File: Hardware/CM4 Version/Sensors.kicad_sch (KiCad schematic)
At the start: 35 parts, among them J10 Conn_01x04, J11 Conn_01x06, J12 TSW-101-08-G-T-RA, J16 Conn_01x03_Female, J4 32K101-400L5, J5 TSW-101-08-G-T-RA, J6 TSW-101-08-G-T-RA, J7 TSW-101-08-G-T-RA, J8 TSW-101-08-G-T-RA, J9 Conn_01x02, Q2 BC817W, U1 BMP280, U2 MAX-M8Q, U3 LSM9DS1

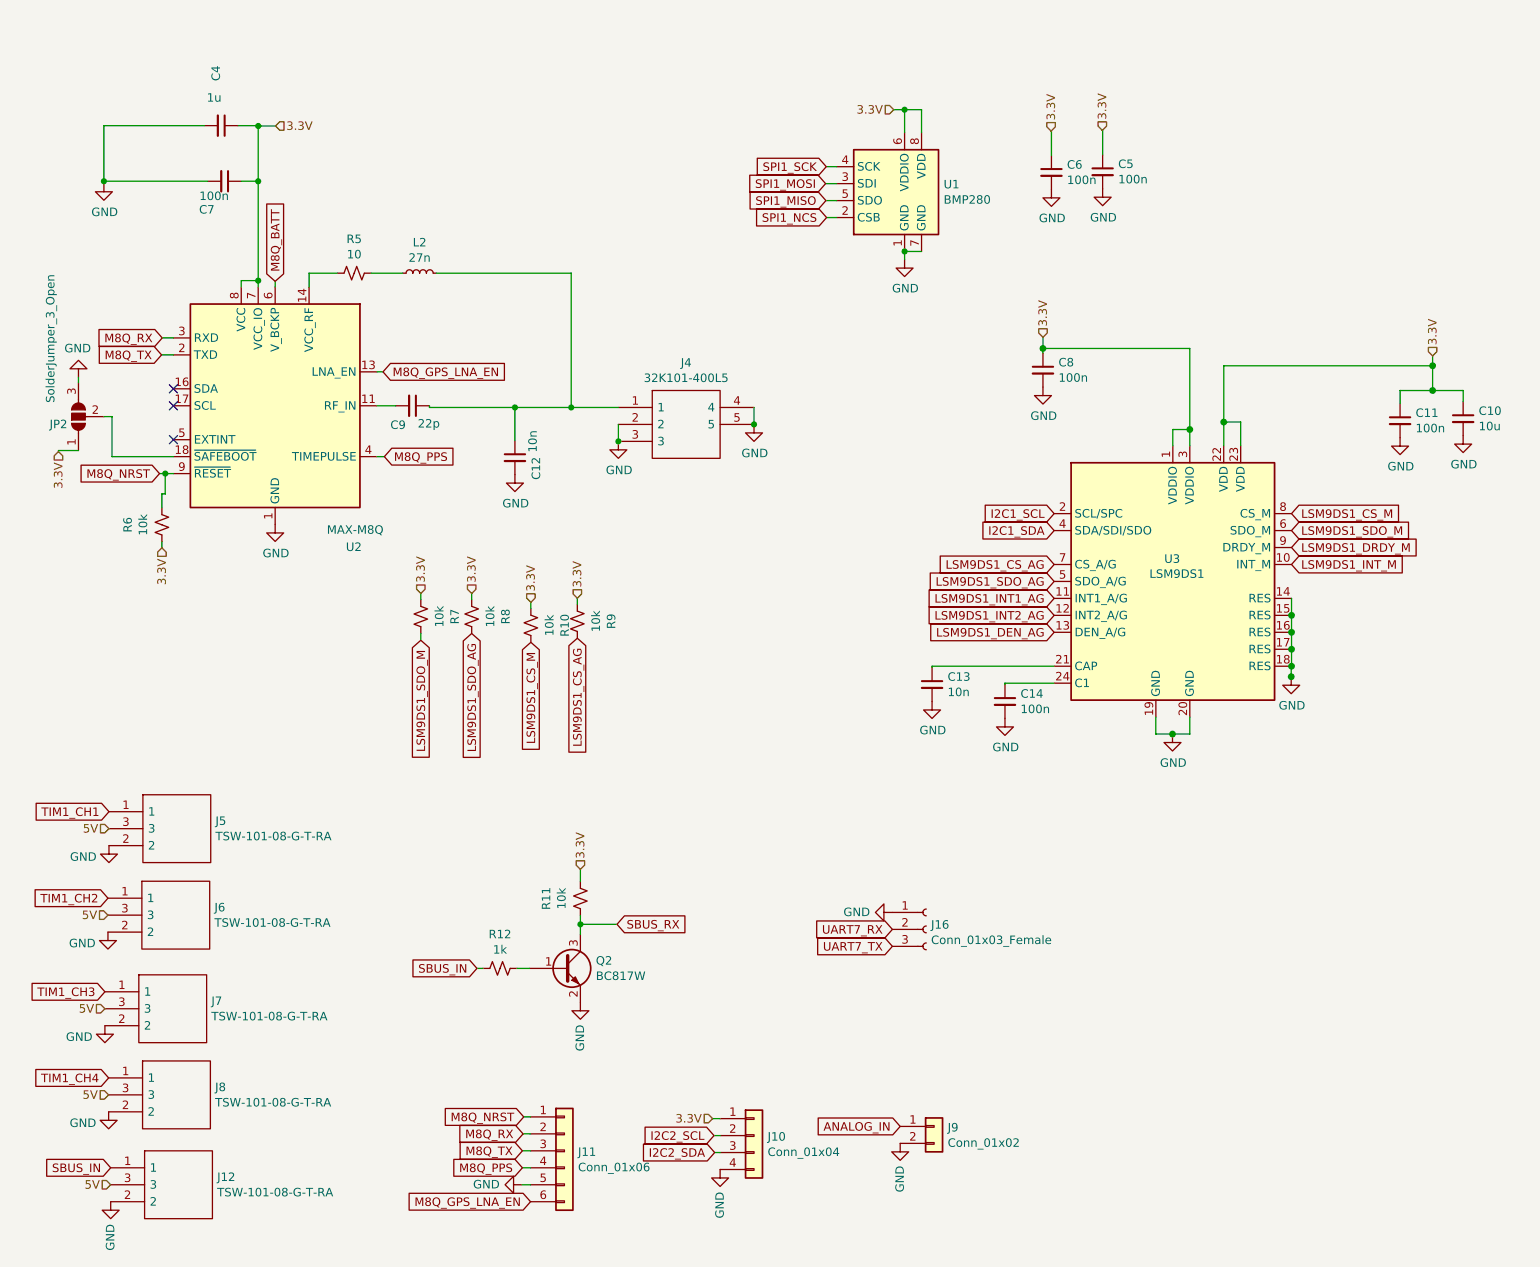
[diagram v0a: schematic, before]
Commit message: Remove CM4-Backups
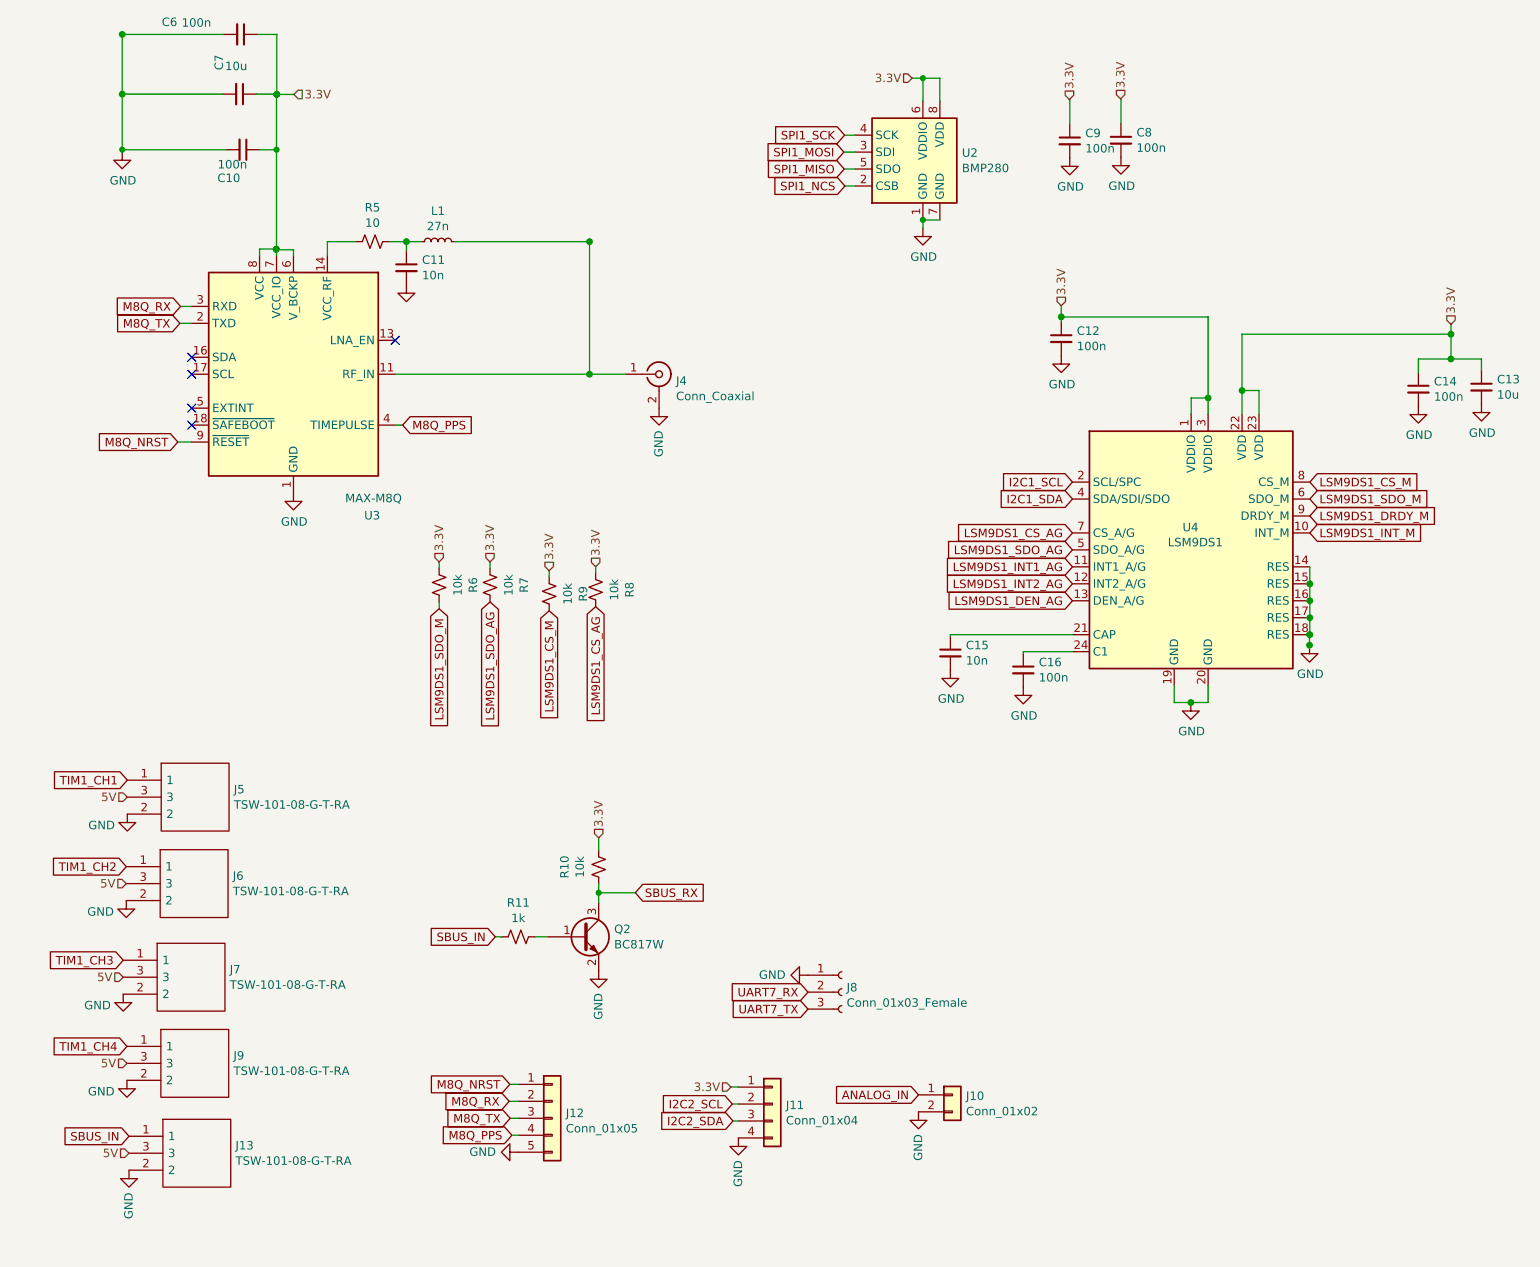
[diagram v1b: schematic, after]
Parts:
- removed C4: 1u, Capacitor_SMD:C_0603_1608Metric, symbol Device:C_Small
- removed C5: 100n, Capacitor_SMD:C_0402_1005Metric, symbol Device:C_Small
- removed J10: Conn_01x04, Connector_Molex:Molex_PicoBlade_53261-0471_1x04-1MP_P1.25mm_Horizontal, symbol Connector_Generic:Conn_01x04
- removed J11: Conn_01x06, Connector_Molex:Molex_PicoBlade_53261-0671_1x06-1MP_P1.25mm_Horizontal, symbol Connector_Generic:Conn_01x06
- removed J12, J8: TSW-101-08-G-T-RA, SamacSys_Parts:HDRRA3W64P254_3X1_254X254X810P, symbol SamacSys_Parts:HTSW-101-08-G-T-RA
- removed J16: Conn_01x03_Female, Connector_PinHeader_2.54mm:PinHeader_1x03_P2.54mm_Vertical, symbol Connector:Conn_01x03_Female
- removed J4: 32K101-400L5, SamacSys_Parts:32K101-400L5, symbol SamacSys_Parts:32K101-400L5
- removed J9: Conn_01x02, Connector_Molex:Molex_PicoBlade_53048-0210_1x02_P1.25mm_Horizontal, symbol Connector_Generic:Conn_01x02
- removed JP2: SolderJumper_3_Open, Jumper:SolderJumper-3_P1.3mm_Open_RoundedPad1.0x1.5mm, symbol Jumper:SolderJumper_3_Open
- removed L2: 27n, Inductor_SMD:L_0402_1005Metric_Pad0.77x0.64mm_HandSolder, symbol Device:L_Small
- removed R12: 1k, Resistor_SMD:R_0402_1005Metric, symbol Device:R_Small_US
- removed U1: BMP280, Package_LGA:Bosch_LGA-8_2x2.5mm_P0.65mm_ClockwisePinNumbering, symbol Sensor_Pressure:BMP280
- removed U2: MAX-M8Q, RF_GPS:ublox_MAX, symbol RF_GPS:MAX-M8Q
- removed U3: LSM9DS1, Package_LGA:LGA-24L_3x3.5mm_P0.43mm, symbol Sensor_Motion:LSM9DS1
- added C15: 10n, Capacitor_SMD:C_0402_1005Metric, symbol Device:C_Small
- added C16: 100n, Capacitor_SMD:C_0402_1005Metric, symbol Device:C_Small
- added J10: Conn_01x02, Connector_Molex:Molex_PicoBlade_53048-0210_1x02_P1.25mm_Horizontal, symbol Connector_Generic:Conn_01x02
- added J11: Conn_01x04, Connector_Molex:Molex_PicoBlade_53261-0471_1x04-1MP_P1.25mm_Horizontal, symbol Connector_Generic:Conn_01x04
- added J12: Conn_01x05, Connector_Molex:Molex_PicoBlade_53047-0510_1x05_P1.25mm_Vertical, symbol Connector_Generic:Conn_01x05
- added J13, J9: TSW-101-08-G-T-RA, SamacSys_Parts:HDRRA3W64P254_3X1_254X254X810P, symbol SamacSys_Parts:HTSW-101-08-G-T-RA
- added J4: Conn_Coaxial, CM4IO:BWIPX-1-001E, symbol Connector:Conn_Coaxial
- added J8: Conn_01x03_Female, Connector_PinHeader_2.54mm:PinHeader_1x03_P2.54mm_Vertical, symbol Connector:Conn_01x03_Female
- added L1: 27n, Inductor_SMD:L_0402_1005Metric_Pad0.77x0.64mm_HandSolder, symbol Device:L_Small
- added U2: BMP280, Package_LGA:Bosch_LGA-8_2x2.5mm_P0.65mm_ClockwisePinNumbering, symbol Sensor_Pressure:BMP280
- added U3: MAX-M8Q, RF_GPS:ublox_MAX, symbol RF_GPS:MAX-M8Q
- added U4: LSM9DS1, Package_LGA:LGA-24L_3x3.5mm_P0.43mm, symbol Sensor_Motion:LSM9DS1
- C10: value 10u -> 100n; footprint Capacitor_SMD:C_0603_1608Metric -> Capacitor_SMD:C_0402_1005Metric; Digi-Key_PN (none) -> 587-1226-2-ND; LCSC Part # (none) -> C1525; Seeed SKU 302010103 -> 302010024
- C11: value 100n -> 10n; Digi-Key_PN 587-1226-2-ND -> (none); LCSC Part # C1525 -> C15195; Seeed SKU 302010024 -> (none)
- C12: value 10n -> 100n; Digi-Key_PN (none) -> 587-1226-2-ND; LCSC Part # (none) -> C1525; Seeed SKU 302010006 -> 302010024
- C13: value 10n -> 10u; footprint Capacitor_SMD:C_0402_1005Metric -> Capacitor_SMD:C_0603_1608Metric; LCSC Part # (none) -> C19702; Seeed SKU 302010006 -> 302010103
- C7: value 100n -> 10u; footprint Capacitor_SMD:C_0402_1005Metric -> Capacitor_SMD:C_0603_1608Metric; Digi-Key_PN 587-1226-2-ND -> (none); LCSC Part # C1525 -> C15849; Seeed SKU 302010024 -> 302010139
- C9: value 22p -> 100n; Digi-Key_PN (none) -> 587-1226-2-ND; LCSC Part # (none) -> C1525; Seeed SKU 302010018 -> 302010024
- J5, J6, J7: Digi-Key_PN SAM12297-ND -> (none)
- Q2: LCSC Part # (none) -> C148104
- R10, R6, R7, R8, R9: LCSC Part # C25744 -> C25744
- R11: value 10k -> 1k; Digi-Key_PN RG10P10.0KDTR-ND -> (none); LCSC Part # C25744 -> C21190; Seeed SKU 301010004 -> 301010006
- R5: LCSC Part # (none) -> C22859
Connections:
- net 3.3V: now also C12.1, C13.1, C14.1, C9.1, R10.2, J11.1 (Pin_1), U2.6 (VDDIO), U2.8 (VDD), U3.6 (V_BCKP), U3.7 (VCC_IO), U3.8 (VCC), U4.1 (VDDIO), U4.22 (VDD), U4.23 (VDD), U4.3 (VDDIO); no longer C11.1, R10.1, R11.2
- net 5V: now also J13.3, J9.3
- net ANALOG_IN: now also J10.1 (Pin_1)
- net GND: now also C9.2, C15.2, C16.2, J10.2 (Pin_2), J11.4 (Pin_4), J12.5 (Pin_5), J13.2, J4.2 (Ext), J8.1 (Pin_1), J9.2, U2.1 (GND), U2.7 (GND), U3.1 (GND), U3.10 (GND), U3.12 (GND), U4.14 (RES), U4.15 (RES), U4.16 (RES), U4.17 (RES), U4.18 (RES), U4.19 (GND), U4.20 (GND)
- net I2C1_SCL: now also U4.2 (SCL/SPC)
- net I2C1_SDA: now also U4.4 (SDA/SDI/SDO)
- net I2C2_SCL: now also J11.2 (Pin_2)
- net I2C2_SDA: now also J11.3 (Pin_3)
- net LSM9DS1_CS_AG: now also R8.2, U4.7 (CS_A/G); no longer R9.2
- net LSM9DS1_CS_M: now also R9.2, U4.8 (CS_M); no longer R10.2
- net LSM9DS1_DEN_AG: now also U4.13 (DEN_A/G)
- net LSM9DS1_DRDY_M: now also U4.9 (DRDY_M)
- net LSM9DS1_INT1_AG: now also U4.11 (INT1_A/G)
- net LSM9DS1_INT2_AG: now also U4.12 (INT2_A/G)
- net LSM9DS1_INT_M: now also U4.10 (INT_M)
- net LSM9DS1_SDO_AG: now also R7.2, U4.5 (SDO_A/G); no longer R8.2
- net LSM9DS1_SDO_M: now also R6.2, U4.6 (SDO_M); no longer R7.2
- net M8Q_NRST: now also J12.1 (Pin_1), U3.9 (~{RESET}); no longer R6.2
- net M8Q_PPS: now also J12.4 (Pin_4), U3.4 (TIMEPULSE)
- net M8Q_RX: now also J12.2 (Pin_2), U3.3 (RXD)
- net M8Q_TX: now also J12.3 (Pin_3), U3.2 (TXD)
- net SBUS_IN: now also R11.1, J13.1
- net SBUS_RX: now also R10.1; no longer R11.1
- net SPI1_MISO: now also U2.5 (SDO)
- net SPI1_MOSI: now also U2.3 (SDI)
- net SPI1_NCS: now also U2.2 (CSB)
- net SPI1_SCK: now also U2.4 (SCK)
- net TIM1_CH4: now also J9.1
- net UART7_RX: now also J8.2 (Pin_2)
- net UART7_TX: now also J8.3 (Pin_3)
- net at Q2.1 (B): now also R11.2
- net at R5.2: now also C11.1, L1.1
- net at R5.1: now also U3.14 (VCC_RF)
- new net: J4.1 (In), L1.2, U3.11 (RF_IN)
- new net: C15.1, U4.21 (CAP)
- new net: C16.1, U4.24 (C1)
- no-connect marks 3 -> 5
